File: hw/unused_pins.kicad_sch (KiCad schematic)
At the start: 0 parts

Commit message: WIP (layout)
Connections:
- no-connect marks 126 -> 124

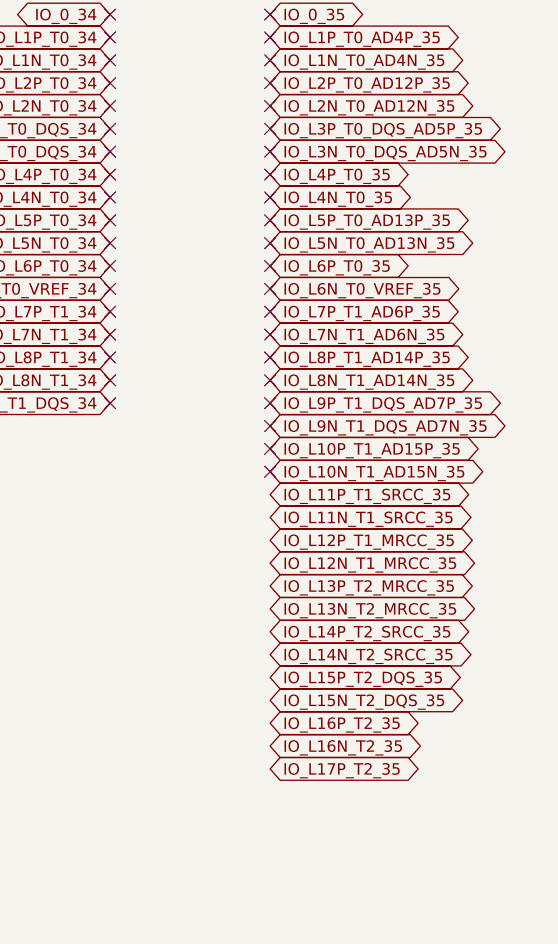
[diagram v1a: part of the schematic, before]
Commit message: connected ulpi PHY
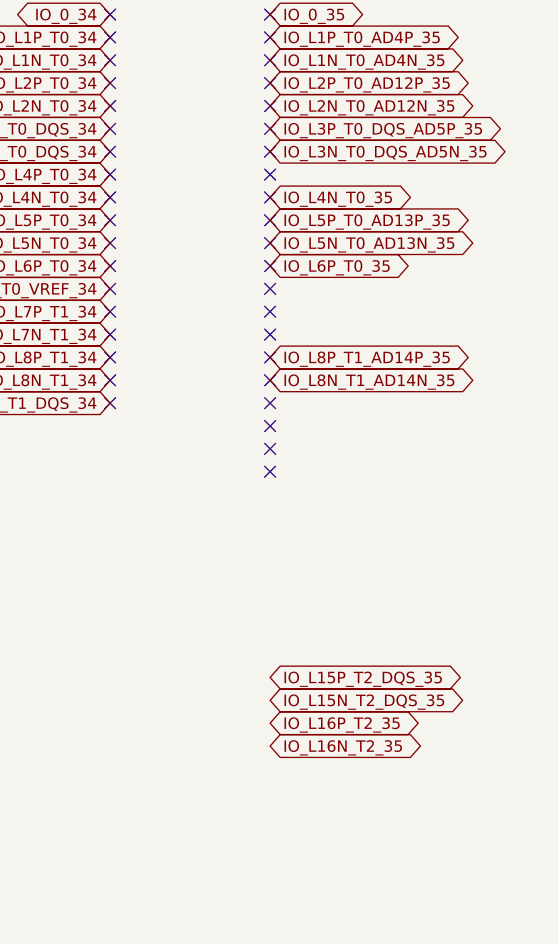
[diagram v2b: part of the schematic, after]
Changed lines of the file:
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@@
-    )
-  )
-  (global_label "IO_L7N_T1_AD6N_35" (shape bidirectional) (at 223.52 66.04 0) (fields_autoplaced)
-    (effects (font (size 1.27 1.27)) (justify left))
-    (property "Intersheetrefs" "${INTERSHEET_REFS}" (at 239.7264 66.04 0)
-      (effects (font (size 1.27 1.27)) (justify left) hide)
     )
   )
@@
     )
   )
-  (global_label "IO_L14N_T2_SRCC_35" (shape bidirectional) (at 223.52 101.6 0) (fields_autoplaced)
-    (effects (font (size 1.27 1.27)) (justify left))
-    (property "Intersheetrefs" "${INTERSHEET_REFS}" (at 246.923 101.6 0)
-      (effects (font (size 1.27 1.27)) (justify left) hide)
-    )
-  )
   (global_label "IO_L2N_T0_AD12N_35" (shape bidirectional) (at 223.52 40.64 0) (fields_autoplaced)
     (effects (font (size 1.27 1.27)) (justify left))
@@
     )
   )
-  (global_label "IO_L11P_T1_SRCC_35" (shape bidirectional) (at 223.52 83.82 0) (fields_autoplaced)
-    (effects (font (size 1.27 1.27)) (justify left))
-    (property "Intersheetrefs" "${INTERSHEET_REFS}" (at 246.8625 83.82 0)
-      (effects (font (size 1.27 1.27)) (justify left) hide)
-    )
-  )
   (global_label "IO_L21P_T3_DQS_14" (shape bidirectional) (at 69.85 134.62 0) (fields_autoplaced)
     (effects (font (size 1.27 1.27)) (justify left))
@@
     )
   )
-  (global_label "IO_L7P_T1_AD6P_35" (shape bidirectional) (at 223.52 63.5 0) (fields_autoplaced)
-    (effects (font (size 1.27 1.27)) (justify left))
-    (property "Intersheetrefs" "${INTERSHEET_REFS}" (at 239.6659 63.5 0)
-      (effects (font (size 1.27 1.27)) (justify left) hide)
-    )
-  )
   (global_label "IO_L4N_T0_34" (shape bidirectional) (at 205.74 50.8 180) (fields_autoplaced)
     (effects (font (size 1.27 1.27)) (justify right))
@@
     )
   )
-  (global_label "IO_L9P_T1_DQS_AD7P_35" (shape bidirectional) (at 223.52 73.66 0) (fields_autoplaced)
-    (effects (font (size 1.27 1.27)) (justify left))
-    (property "Intersheetrefs" "${INTERSHEET_REFS}" (at 244.4435 73.66 0)
-      (effects (font (size 1.27 1.27)) (justify left) hide)
-    )
-  )
   (global_label "IO_L3P_T0_DQS_AD1P_15" (shape bidirectional) (at 57.15 43.18 180) (fields_autoplaced)
     (effects (font (size 1.27 1.27)) (justify right))
@@
     )
   )
-  (global_label "IO_L6N_T0_VREF_35" (shape bidirectional) (at 223.52 60.96 0) (fields_autoplaced)
-    (effects (font (size 1.27 1.27)) (justify left))
-    (property "Intersheetrefs" "${INTERSHEET_REFS}" (at 245.2902 60.96 0)
-      (effects (font (size 1.27 1.27)) (justify left) hide)
-    )
-  )
   (global_label "IO_L2P_T0_D02_14" (shape bidirectional) (at 69.85 38.1 0) (fields_autoplaced)
     (effects (font (size 1.27 1.27)) (justify left))
@@
     )
   )
-  (global_label "IO_L12N_T1_MRCC_35" (shape bidirectional) (at 223.52 91.44 0) (fields_autoplaced)
-    (effects (font (size 1.27 1.27)) (justify left))
-    (property "Intersheetrefs" "${INTERSHEET_REFS}" (at 247.1649 91.44 0)
-      (effects (font (size 1.27 1.27)) (justify left) hide)
-    )
-  )
   (global_label "IO_L5N_T0_AD9N_15" (shape bidirectional) (at 57.15 55.88 180) (fields_autoplaced)
     (effects (font (size 1.27 1.27)) (justify right))
@@
     )
   )
-  (global_label "IO_L10P_T1_AD15P_35" (shape bidirectional) (at 223.52 78.74 0) (fields_autoplaced)
-    (effects (font (size 1.27 1.27)) (justify left))
-    (property "Intersheetrefs" "${INTERSHEET_REFS}" (at 240.8754 78.74 0)
-      (effects (font (size 1.27 1.27)) (justify left) hide)
-    )
-  )
   (global_label "IO_L7N_T1_D10_14" (shape bidirectional) (at 69.85 66.04 0) (fields_autoplaced)
     (effects (font (size 1.27 1.27)) (justify left))
@@
     )
   )
-  (global_label "IO_L4P_T0_35" (shape bidirectional) (at 223.52 48.26 0) (fields_autoplaced)
-    (effects (font (size 1.27 1.27)) (justify left))
-    (property "Intersheetrefs" "${INTERSHEET_REFS}" (at 239.6659 48.26 0)
-      (effects (font (size 1.27 1.27)) (justify left) hide)
-    )
-  )
   (global_label "IO_0_34" (shape bidirectional) (at 205.74 30.48 180) (fields_autoplaced)
     (effects (font (size 1.27 1.27)) (justify right))
@@
     )
   )
-  (global_label "IO_L9N_T1_DQS_AD7N_35" (shape bidirectional) (at 223.52 76.2 0) (fields_autoplaced)
-    (effects (font (size 1.27 1.27)) (justify left))
-    (property "Intersheetrefs" "${INTERSHEET_REFS}" (at 244.504 76.2 0)
-      (effects (font (size 1.27 1.27)) (justify left) hide)
-    )
-  )
   (global_label "IO_L16N_T2_A27_15" (shape bidirectional) (at 57.15 111.76 180) (fields_autoplaced)
     (effects (font (size 1.27 1.27)) (justify right))
@@
     )
   )
-  (global_label "IO_L10N_T1_AD15N_35" (shape bidirectional) (at 223.52 81.28 0) (fields_autoplaced)
-    (effects (font (size 1.27 1.27)) (justify left))
-    (property "Intersheetrefs" "${INTERSHEET_REFS}" (at 240.9359 81.28 0)
-      (effects (font (size 1.27 1.27)) (justify left) hide)
-    )
-  )
   (global_label "IO_L4N_T0_D05_14" (shape bidirectional) (at 69.85 50.8 0) (fields_autoplaced)
     (effects (font (size 1.27 1.27)) (justify left))
@@
     )
   )
-  (global_label "IO_L12P_T1_MRCC_35" (shape bidirectional) (at 223.52 88.9 0) (fields_autoplaced)
-    (effects (font (size 1.27 1.27)) (justify left))
-    (property "Intersheetrefs" "${INTERSHEET_REFS}" (at 247.1044 88.9 0)
-      (effects (font (size 1.27 1.27)) (justify left) hide)
-    )
-  )
   (global_label "IO_25_14" (shape bidirectional) (at 69.85 154.94 0) (fields_autoplaced)
     (effects (font (size 1.27 1.27)) (justify left))
@@
     )
   )
-  (global_label "IO_L14P_T2_SRCC_35" (shape bidirectional) (at 223.52 99.06 0) (fields_autoplaced)
-    (effects (font (size 1.27 1.27)) (justify left))
-    (property "Intersheetrefs" "${INTERSHEET_REFS}" (at 246.8625 99.06 0)
-      (effects (font (size 1.27 1.27)) (justify left) hide)
-    )
-  )
   (global_label "IO_L11N_T1_SRCC_15" (shape bidirectional) (at 57.15 86.36 180) (fields_autoplaced)
     (effects (font (size 1.27 1.27)) (justify right))
@@
     )
   )
-  (global_label "IO_L13N_T2_MRCC_35" (shape bidirectional) (at 223.52 96.52 0) (fields_autoplaced)
-    (effects (font (size 1.27 1.27)) (justify left))
-    (property "Intersheetrefs" "${INTERSHEET_REFS}" (at 247.1649 96.52 0)
-      (effects (font (size 1.27 1.27)) (justify left) hide)
-    )
-  )
-  (global_label "IO_L17P_T2_35" (shape bidirectional) (at 223.52 114.3 0) (fields_autoplaced)
-    (effects (font (size 1.27 1.27)) (justify left))
-    (property "Intersheetrefs" "${INTERSHEET_REFS}" (at 240.8754 114.3 0)
-      (effects (font (size 1.27 1.27)) (justify left) hide)
-    )
-  )
-  (global_label "IO_L13P_T2_MRCC_35" (shape bidirectional) (at 223.52 93.98 0) (fields_autoplaced)
-    (effects (font (size 1.27 1.27)) (justify left))
-    (property "Intersheetrefs" "${INTERSHEET_REFS}" (at 247.1044 93.98 0)
-      (effects (font (size 1.27 1.27)) (justify left) hide)
-    )
-  )
   (global_label "IO_L1P_T0_AD4P_35" (shape bidirectional) (at 223.52 33.02 0) (fields_autoplaced)
     (effects (font (size 1.27 1.27)) (justify left))
@@
       (effects (font (size 1.27 1.27)) (justify left) hide)
     )
-  )
-  (global_label "IO_L11N_T1_SRCC_35" (shape bidirectional) (at 223.52 86.36 0) (fields_autoplaced)
-    (effects (font (size 1.27 1.27)) (justify left))
-    (property "Intersheetrefs" "${INTERSHEET_REFS}" (at 246.923 86.36 0)
-      (effects (font (size 1.27 1.27)) (justify left) hide)
-    )

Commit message: WIP - a lot already laid out.
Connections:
- no-connect marks 124 -> 153

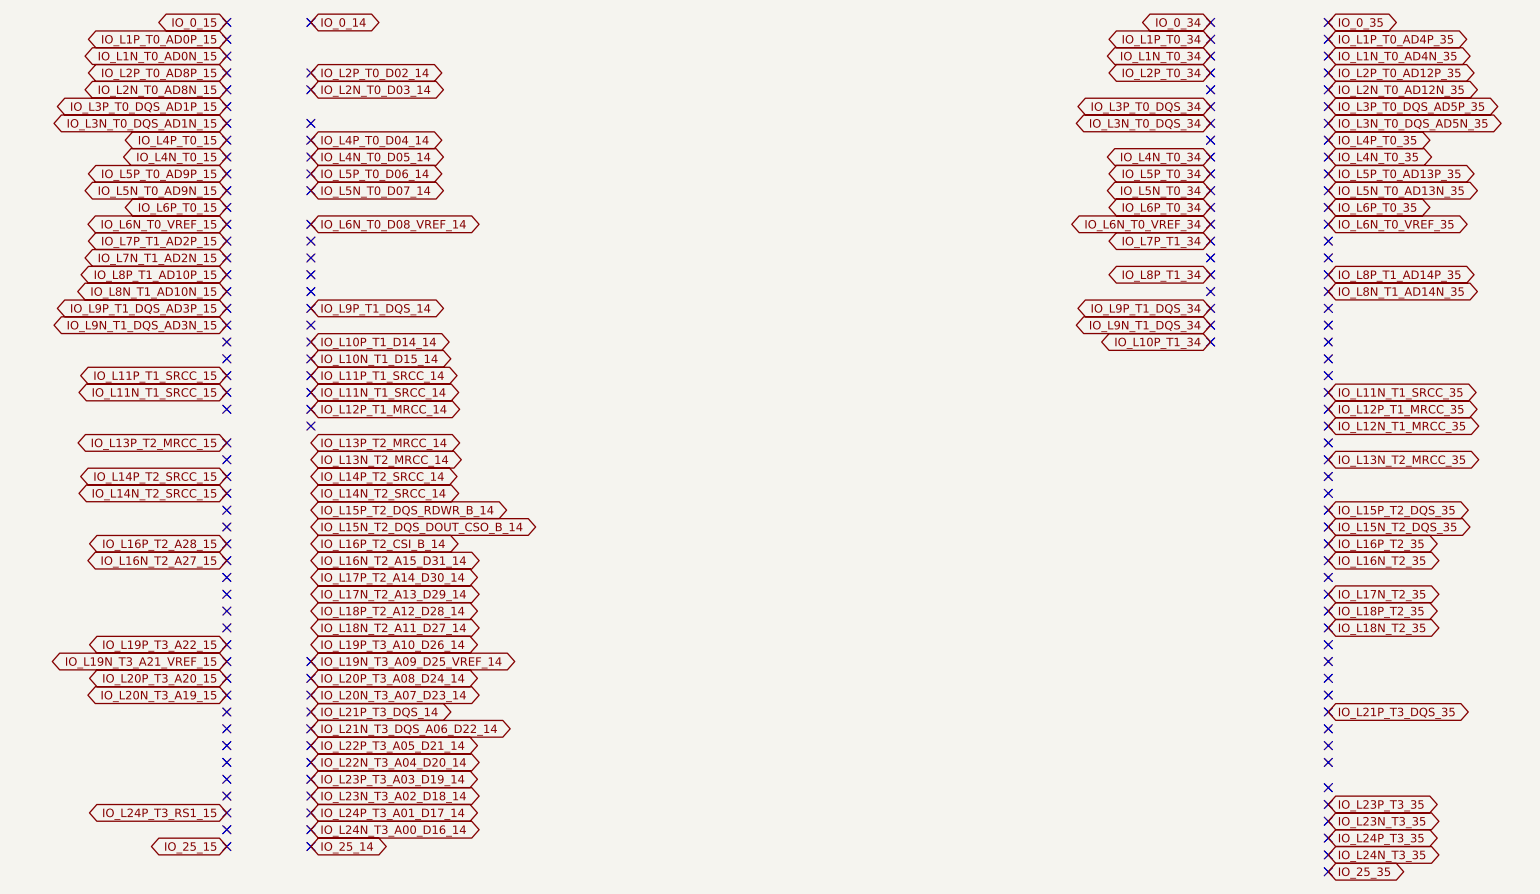
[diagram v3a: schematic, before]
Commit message: WIP - almost everything except power (converters) connected
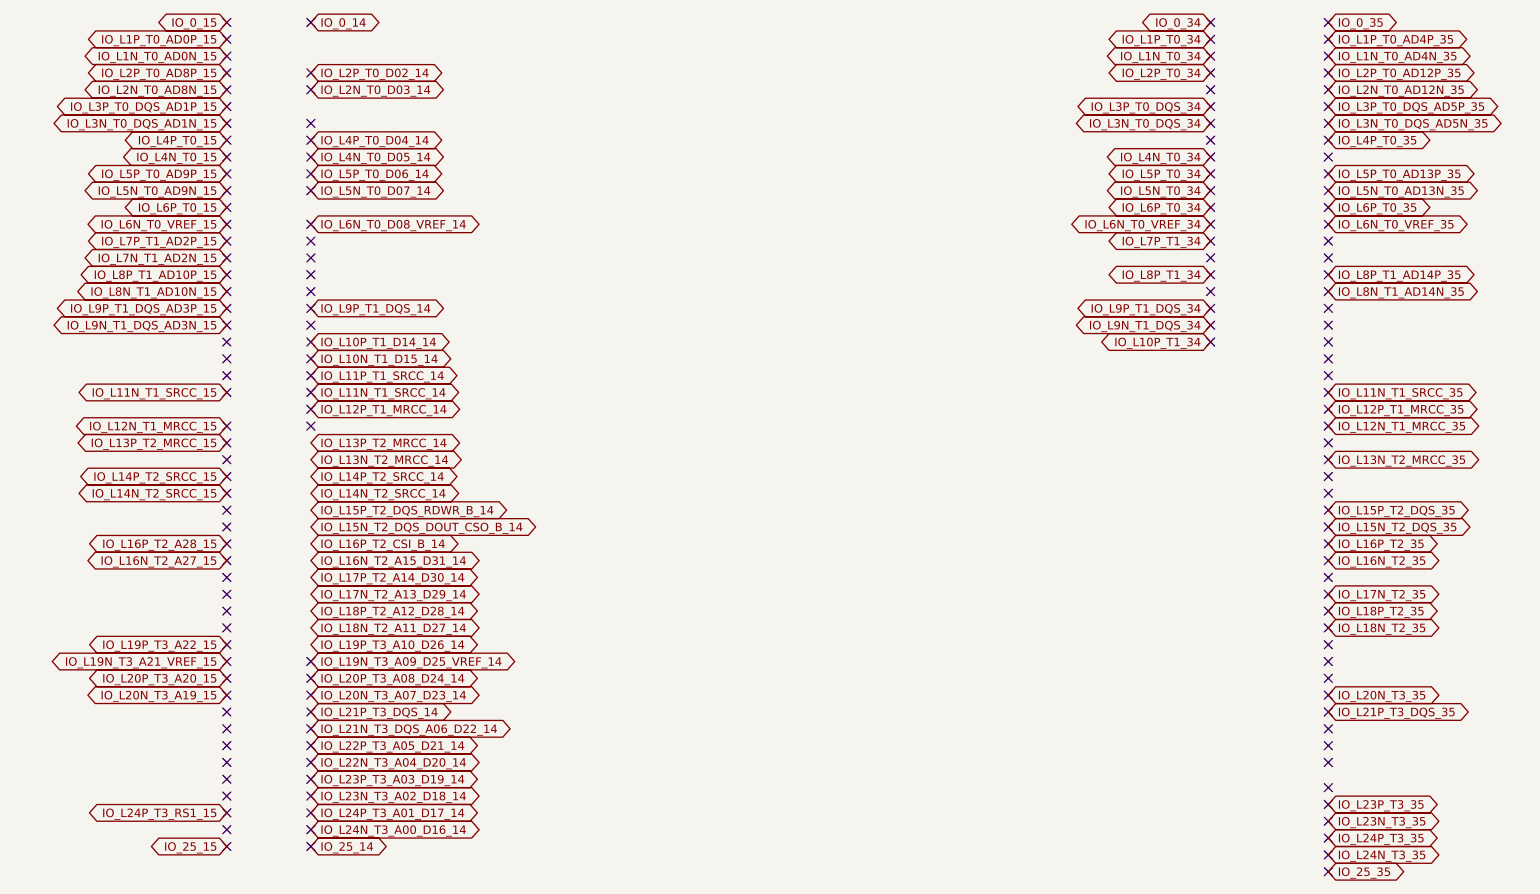
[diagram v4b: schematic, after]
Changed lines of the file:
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@@
   (no_connect (at 69.85 91.44))
   (no_connect (at 57.15 99.06))
-  (no_connect (at 57.15 88.9))
+  (no_connect (at 57.15 91.44))
   (no_connect (at 69.85 30.48))
   (no_connect (at 223.52 146.05))
@@
     )
   )
-  (global_label "IO_L11P_T1_SRCC_15" (shape bidirectional) (at 57.15 83.82 180) (fields_autoplaced)
-    (effects (font (size 1.27 1.27)) (justify right))
-    (property "Intersheetrefs" "${INTERSHEET_REFS}" (at 33.8075 83.82 0)
-      (effects (font (size 1.27 1.27)) (justify right) hide)
-    )
-  )
   (global_label "IO_L16N_T2_35" (shape bidirectional) (at 223.52 111.76 0) (fields_autoplaced)
     (effects (font (size 1.27 1.27)) (justify left))
@@
     )
   )
-  (global_label "IO_L4N_T0_35" (shape bidirectional) (at 223.52 50.8 0) (fields_autoplaced)
-    (effects (font (size 1.27 1.27)) (justify left))
-    (property "Intersheetrefs" "${INTERSHEET_REFS}" (at 239.7264 50.8 0)
-      (effects (font (size 1.27 1.27)) (justify left) hide)
-    )
-  )
   (global_label "IO_L9N_T1_DQS_AD3N_15" (shape bidirectional) (at 57.15 76.2 180) (fields_autoplaced)
     (effects (font (size 1.27 1.27)) (justify right))
@@
     )
   )
+  (global_label "IO_L12N_T1_MRCC_15" (shape bidirectional) (at 57.15 91.44 180) (fields_autoplaced)
+    (effects (font (size 1.27 1.27)) (justify right))
+    (property "Intersheetrefs" "${INTERSHEET_REFS}" (at 33.5051 91.44 0)
+      (effects (font (size 1.27 1.27)) (justify right) hide)
+    )
+  )
   (global_label "IO_L1N_T0_AD4N_35" (shape bidirectional) (at 223.52 35.56 0) (fields_autoplaced)
     (effects (font (size 1.27 1.27)) (justify left))
@@
     )
   )
+  (global_label "IO_L20N_T3_35" (shape bidirectional) (at 223.52 132.08 0) (fields_autoplaced)
+    (effects (font (size 1.27 1.27)) (justify left))
+    (property "Intersheetrefs" "${INTERSHEET_REFS}" (at 240.9359 132.08 0)
+      (effects (font (size 1.27 1.27)) (justify left) hide)
+    )
+  )

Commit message: layout finished (draft)
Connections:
- no-connect marks 153 -> 117
